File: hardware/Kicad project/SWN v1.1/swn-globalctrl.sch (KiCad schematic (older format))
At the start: 159 parts, among them IC11 TLV171, IC12 TL082, IC13 TL082, IC6 TL082, IC8 TL082, IC9 TL082, SW1 submini-3T, SW2 submini-2T

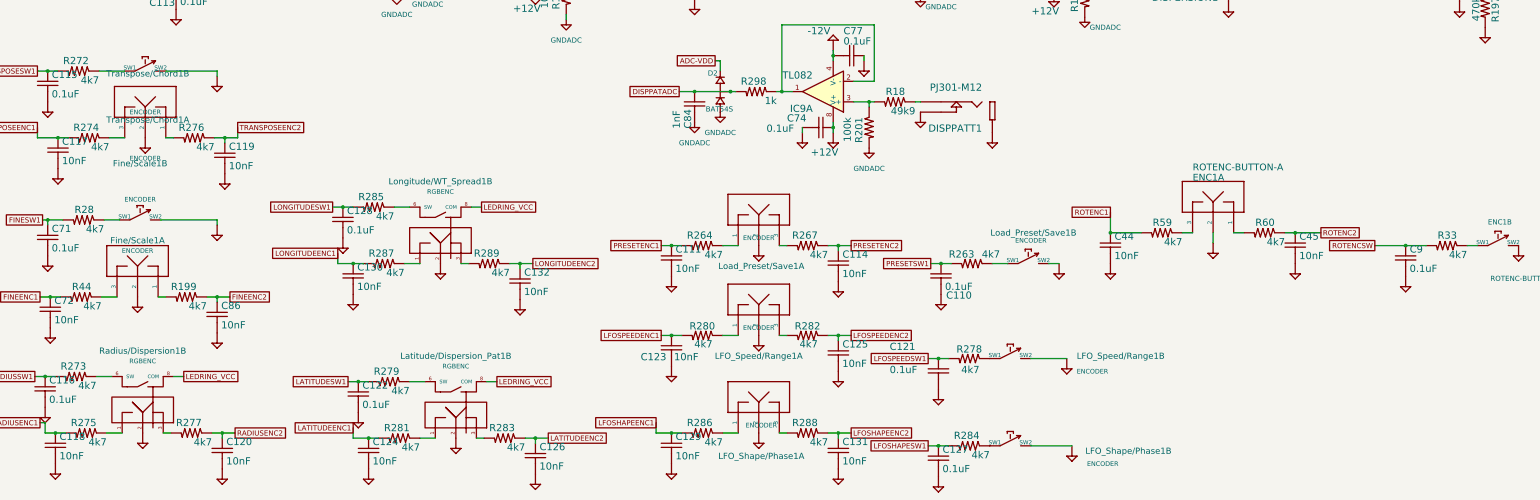
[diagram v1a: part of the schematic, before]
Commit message: 4k7 -> 10k for global control schematic resistors
There's a disparity between the resistors in these positions between the schematic and the PCB. I cross referenced this against the product photos on the 4ms website and it appears as though the PCB is correct, so I adjusted all but two of the 4k7 resistors in this schematic to match the PCB.
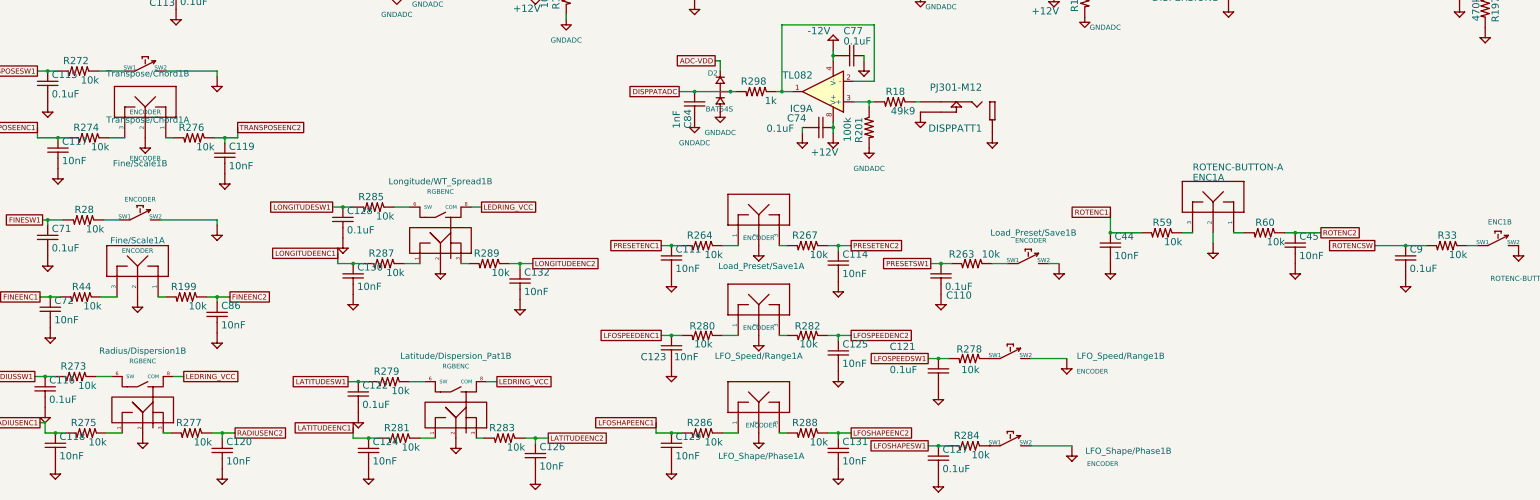
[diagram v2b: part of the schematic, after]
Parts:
- R199, R263, R264, R267, R272, R273, R274, R275, R276, R277, R278, R279, R28, R280, R281, R282, R283, R284, R285, R286, R287, R288, R289, R33, R44, R59, R60: value 4k7 -> 10k
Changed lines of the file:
@@
 P 14825 8100
 F 0 "R33" H 14725 8159 70  0000 L BNN
-F 1 "4k7" H 14625 7970 70  0000 L BNN
+F 1 "10k" H 14625 7970 70  0000 L BNN
 F 2 "4ms-footprints:R0603" H 14815 7890 65  0001 L TNN
 F 3 "" H 14825 8100 60  0001 C CNN
@@
 P 12050 7975
 F 0 "R59" H 11950 8034 70  0000 L BNN
-F 1 "4k7" H 11850 7845 70  0000 L BNN
+F 1 "10k" H 11850 7845 70  0000 L BNN
 F 2 "4ms-footprints:R0603" H 12040 7765 65  0001 L TNN
 F 3 "" H 12050 7975 60  0001 C CNN
@@
 P 13050 7975
 F 0 "R60" H 12950 8034 70  0000 L BNN
-F 1 "4k7" H 12850 7845 70  0000 L BNN
+F 1 "10k" H 12850 7845 70  0000 L BNN
 F 2 "4ms-footprints:R0603" H 13040 7765 65  0001 L TNN
 F 3 "" H 13050 7975 60  0001 C CNN
@@
 P 1525 8600
 F 0 "R44" H 1425 8659 70  0000 L BNN
-F 1 "4k7" H 1325 8470 70  0000 L BNN
+F 1 "10k" H 1325 8470 70  0000 L BNN
 F 2 "4ms-footprints:R0603" H 1515 8390 65  0001 L TNN
 F 3 "" H 1525 8600 60  0001 C CNN
@@
 P 2550 8600
 F 0 "R199" H 2450 8659 70  0000 L BNN
-F 1 "4k7" H 2350 8470 70  0000 L BNN
+F 1 "10k" H 2350 8470 70  0000 L BNN
 F 2 "4ms-footprints:R0603" H 2540 8390 65  0001 L TNN
 F 3 "" H 2550 8600 60  0001 C CNN
@@
 P 1550 7850
 F 0 "R28" H 1450 7909 70  0000 L BNN
-F 1 "4k7" H 1350 7720 70  0000 L BNN
+F 1 "10k" H 1350 7720 70  0000 L BNN
 F 2 "4ms-footprints:R0603" H 1540 7640 65  0001 L TNN
 F 3 "" H 1550 7850 60  0001 C CNN
@@
 P 1600 7050
 F 0 "R274" H 1500 7109 70  0000 L BNN
-F 1 "4k7" H 1400 6920 70  0000 L BNN
+F 1 "10k" H 1400 6920 70  0000 L BNN
 F 2 "4ms-footprints:R0603" H 1590 6840 65  0001 L TNN
 F 3 "" H 1600 7050 60  0001 C CNN
@@
 P 2625 7050
 F 0 "R276" H 2525 7109 70  0000 L BNN
-F 1 "4k7" H 2425 6920 70  0000 L BNN
+F 1 "10k" H 2425 6920 70  0000 L BNN
 F 2 "4ms-footprints:R0603" H 2615 6840 65  0001 L TNN
 F 3 "" H 2625 7050 60  0001 C CNN
@@
 P 1500 6400
 F 0 "R272" H 1400 6459 70  0000 L BNN
-F 1 "4k7" H 1300 6270 70  0000 L BNN
+F 1 "10k" H 1300 6270 70  0000 L BNN
 F 2 "4ms-footprints:R0603" H 1490 6190 65  0001 L TNN
 F 3 "" H 1500 6400 60  0001 C CNN
@@
 P 7575 8975
 F 0 "R280" H 7450 9025 70  0000 L BNN
-F 1 "4k7" H 7475 8850 70  0000 L BNN
+F 1 "10k" H 7475 8850 70  0000 L BNN
 F 2 "4ms-footprints:R0603" H 7565 8765 65  0001 L TNN
 F 3 "" H 7575 8975 60  0001 C CNN
@@
 P 8600 8975
 F 0 "R282" H 8475 9025 70  0000 L BNN
-F 1 "4k7" H 8500 8850 70  0000 L BNN
+F 1 "10k" H 8500 8850 70  0000 L BNN
 F 2 "4ms-footprints:R0603" H 8590 8765 65  0001 L TNN
 F 3 "" H 8600 8975 60  0001 C CNN
@@
 P 10175 9200
 F 0 "R278" H 10050 9250 70  0000 L BNN
-F 1 "4k7" H 10075 9050 70  0000 L BNN
+F 1 "10k" H 10075 9050 70  0000 L BNN
 F 2 "4ms-footprints:R0603" H 10165 8990 65  0001 L TNN
 F 3 "" H 10175 9200 60  0001 C CNN
@@
 P 7575 9925
 F 0 "R286" H 7475 9984 70  0000 L BNN
-F 1 "4k7" H 7375 9795 70  0000 L BNN
+F 1 "10k" H 7375 9795 70  0000 L BNN
 F 2 "4ms-footprints:R0603" H 7565 9715 65  0001 L TNN
 F 3 "" H 7575 9925 60  0001 C CNN
@@
 P 8600 9925
 F 0 "R288" H 8500 9984 70  0000 L BNN
-F 1 "4k7" H 8400 9795 70  0000 L BNN
+F 1 "10k" H 8400 9795 70  0000 L BNN
 F 2 "4ms-footprints:R0603" H 8590 9715 65  0001 L TNN
 F 3 "" H 8600 9925 60  0001 C CNN
@@
 P 10175 10050
 F 0 "R284" H 10075 10109 70  0000 L BNN
-F 1 "4k7" H 9975 9920 70  0000 L BNN
+F 1 "10k" H 9975 9920 70  0000 L BNN
 F 2 "4ms-footprints:R0603" H 10165 9840 65  0001 L TNN
 F 3 "" H 10175 10050 60  0001 C CNN
@@
 P 7575 8100
 F 0 "R264" H 7475 8159 70  0000 L BNN
-F 1 "4k7" H 7375 7970 70  0000 L BNN
+F 1 "10k" H 7375 7970 70  0000 L BNN
 F 2 "4ms-footprints:R0603" H 7565 7890 65  0001 L TNN
 F 3 "" H 7575 8100 60  0001 C CNN
@@
 P 8600 8100
 F 0 "R267" H 8500 8159 70  0000 L BNN
-F 1 "4k7" H 8400 7970 70  0000 L BNN
+F 1 "10k" H 8400 7970 70  0000 L BNN
 F 2 "4ms-footprints:R0603" H 8590 7890 65  0001 L TNN
 F 3 "" H 8600 8100 60  0001 C CNN
@@
 P 10200 8275
 F 0 "R263" H 10175 8325 70  0000 L BNN
-F 1 "4k7" H 9925 8325 70  0000 L BNN
+F 1 "10k" H 9925 8325 70  0000 L BNN
 F 2 "4ms-footprints:R0603" H 10190 8065 65  0001 L TNN
 F 3 "" H 10200 8275 60  0001 C CNN
@@
 P 1575 9925
 F 0 "R275" H 1475 9984 70  0000 L BNN
-F 1 "4k7" H 1375 9795 70  0000 L BNN
+F 1 "10k" H 1375 9795 70  0000 L BNN
 F 2 "4ms-footprints:R0603" H 1565 9715 65  0001 L TNN
 F 3 "" H 1575 9925 60  0001 C CNN
@@
 P 2600 9925
 F 0 "R277" H 2500 9984 70  0000 L BNN
-F 1 "4k7" H 2400 9795 70  0000 L BNN
+F 1 "10k" H 2400 9795 70  0000 L BNN
 F 2 "4ms-footprints:R0603" H 2590 9715 65  0001 L TNN
 F 3 "" H 2600 9925 60  0001 C CNN
@@
 P 1475 9375
 F 0 "R273" H 1375 9434 70  0000 L BNN
-F 1 "4k7" H 1275 9245 70  0000 L BNN
+F 1 "10k" H 1275 9245 70  0000 L BNN
 F 2 "4ms-footprints:R0603" H 1465 9165 65  0001 L TNN
 F 3 "" H 1475 9375 60  0001 C CNN
@@
 P 4625 9975
 F 0 "R281" H 4525 10034 70  0000 L BNN
-F 1 "4k7" H 4425 9845 70  0000 L BNN
+F 1 "10k" H 4425 9845 70  0000 L BNN
 F 2 "4ms-footprints:R0603" H 4615 9765 65  0001 L TNN
 F 3 "" H 4625 9975 60  0001 C CNN
@@
 P 5650 9975
 F 0 "R283" H 5550 10034 70  0000 L BNN
-F 1 "4k7" H 5450 9845 70  0000 L BNN
+F 1 "10k" H 5450 9845 70  0000 L BNN
 F 2 "4ms-footprints:R0603" H 5640 9765 65  0001 L TNN
 F 3 "" H 5650 9975 60  0001 C CNN
@@
 P 4525 9425
 F 0 "R279" H 4425 9484 70  0000 L BNN
-F 1 "4k7" H 4325 9295 70  0000 L BNN
+F 1 "10k" H 4325 9295 70  0000 L BNN
 F 2 "4ms-footprints:R0603" H 4515 9215 65  0001 L TNN
 F 3 "" H 4525 9425 60  0001 C CNN
@@
 P 4475 8275
 F 0 "R287" H 4375 8334 70  0000 L BNN
-F 1 "4k7" H 4275 8145 70  0000 L BNN
+F 1 "10k" H 4275 8145 70  0000 L BNN
 F 2 "4ms-footprints:R0603" H 4465 8065 65  0001 L TNN
 F 3 "" H 4475 8275 60  0001 C CNN
@@
 P 5500 8275
 F 0 "R289" H 5400 8334 70  0000 L BNN
-F 1 "4k7" H 5300 8145 70  0000 L BNN
+F 1 "10k" H 5300 8145 70  0000 L BNN
 F 2 "4ms-footprints:R0603" H 5490 8065 65  0001 L TNN
 F 3 "" H 5500 8275 60  0001 C CNN
@@
 P 4375 7725
 F 0 "R285" H 4275 7784 70  0000 L BNN
-F 1 "4k7" H 4175 7595 70  0000 L BNN
+F 1 "10k" H 4175 7595 70  0000 L BNN
 F 2 "4ms-footprints:R0603" H 4365 7515 65  0001 L TNN
 F 3 "" H 4375 7725 60  0001 C CNN
